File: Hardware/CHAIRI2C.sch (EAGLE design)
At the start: 23 parts, among them IC1 DS3502, IC2 DS3502, J2 OUTPUT, J4 M06-PLAIN

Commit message: Changed I2C pullups from 10K to 4K7. Moved designators to improve readability.
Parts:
- R10, R9: value 22K -> 4K7
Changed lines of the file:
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@@
 <part name="GND7" library="SuperHouse-SupplySymbols" library_urn="urn:adsk.eagle:library:11790503" deviceset="GND" device=""/>
 <part name="P+4" library="SuperHouse-SupplySymbols" library_urn="urn:adsk.eagle:library:11790503" deviceset="VCC" device=""/>
-<part name="R9" library="SuperHouse-DiscreteSemi" library_urn="urn:adsk.eagle:library:11768461" deviceset="RESISTOR" device="0603" package3d_urn="urn:adsk.eagle:package:11768543/2" value="22K"/>
-<part name="R10" library="SuperHouse-DiscreteSemi" library_urn="urn:adsk.eagle:library:11768461" deviceset="RESISTOR" device="0603" package3d_urn="urn:adsk.eagle:package:11768543/2" value="22K"/>
+<part name="R9" library="SuperHouse-DiscreteSemi" library_urn="urn:adsk.eagle:library:11768461" deviceset="RESISTOR" device="0603" package3d_urn="urn:adsk.eagle:package:11768543/2" value="4K7"/>
+<part name="R10" library="SuperHouse-DiscreteSemi" library_urn="urn:adsk.eagle:library:11768461" deviceset="RESISTOR" device="0603" package3d_urn="urn:adsk.eagle:package:11768543/2" value="4K7"/>
 <part name="U$2" library="SuperHouse-Jumpers" library_urn="urn:adsk.eagle:library:12190622" deviceset="SJC" device="-NORMAL" package3d_urn="urn:adsk.eagle:package:7066342/1" value="PU"/>
 <part name="U$3" library="SuperHouse-Jumpers" library_urn="urn:adsk.eagle:library:12190622" deviceset="SJC" device="-NORMAL" package3d_urn="urn:adsk.eagle:package:7066342/1" value="PU"/>

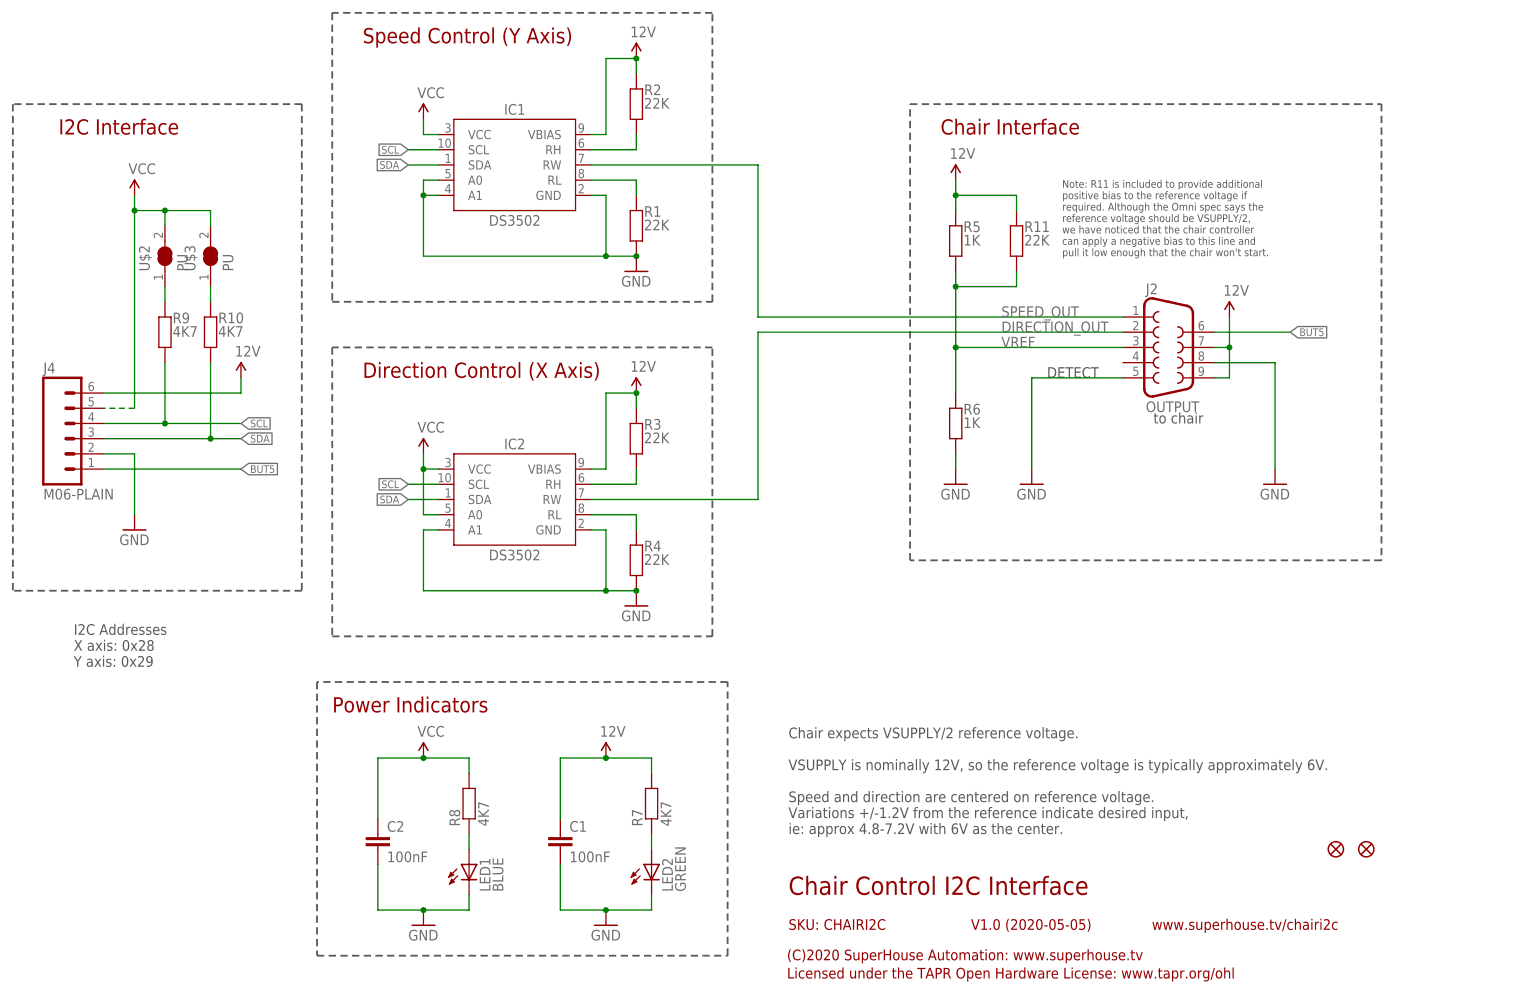
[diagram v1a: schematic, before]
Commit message: Renumbered parts to simplify production setup.
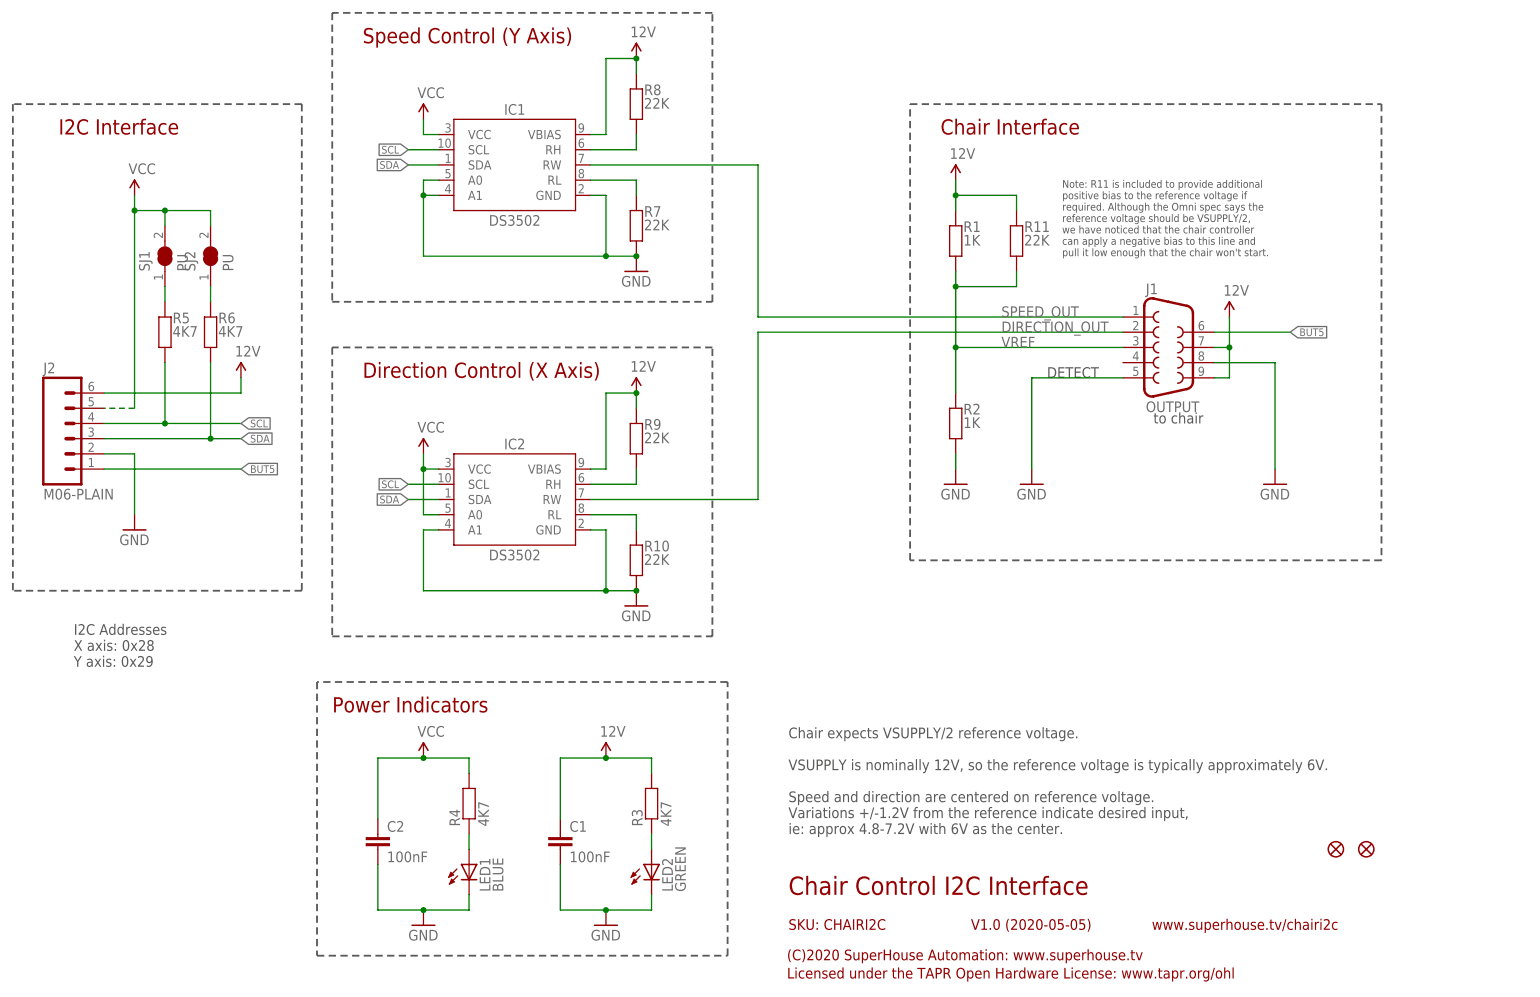
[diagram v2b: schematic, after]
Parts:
- removed J4: M06-PLAIN, SuperHouse-Connectors:M06-PLAIN
- added J1: OUTPUT, SuperHouse-Connectors:DB9-PCB-SOCKET
- J2: value OUTPUT -> M06-PLAIN; device SuperHouse-Connectors:DB9-PCB-SOCKET -> SuperHouse-Connectors:M06-PLAIN
- R1, R2: value 22K -> 1K
- R10, R7, R8, R9: value 4K7 -> 22K
- R3, R4: value 22K -> 4K7
- R5, R6: value 1K -> 4K7
- renumbered U$2 to SJ1, U$3 to SJ2, U$8 to FID1, U$9 to FID2
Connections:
- net 12V: now also J1.7, J1.9, J2.6, R1.2, R8.2, R9.2; no longer J2.7, J2.9, J4.6, R2.2, R5.2, R7.2
- net BUT5: now also J1.6, J2.1; no longer J2.6, J4.1
- net DIRECTION_OUT: now also J1.2; no longer J2.2
- net GND: now also J1.5, J1.8, J2.2, R10.1, R2.1, R7.1; no longer J2.5, J2.8, J4.2, R1.1, R4.1, R6.1
- net N$1: now also R5.2; no longer R9.2
- net N$15: now also R10.2; no longer R4.2
- net N$2: now also R8.1; no longer R2.1
- net N$3: now also R9.1; no longer R3.1
- net N$4: now also R7.2; no longer R1.2
- net N$5: now also R4.1; no longer R8.1
- net N$6: now also R3.1; no longer R7.1
- net N$8: now also R6.2; no longer R10.2
- net SCL: now also J2.4, R5.1; no longer J4.4, R9.1
- net SDA: now also J2.3, R6.1; no longer J4.3, R10.1
- net SPEED_OUT: now also J1.1; no longer J2.1
- net VCC: now also J2.5, R4.2; no longer J4.5, R8.2
- net VREF: now also J1.3, R1.1, R2.2; no longer J2.3, R5.1, R6.2
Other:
- moved on the sheet: R1, R10, R2, R3, R4, R5, R6, R7, R8, R9

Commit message: Changed output range resistors from 22K to 0R.
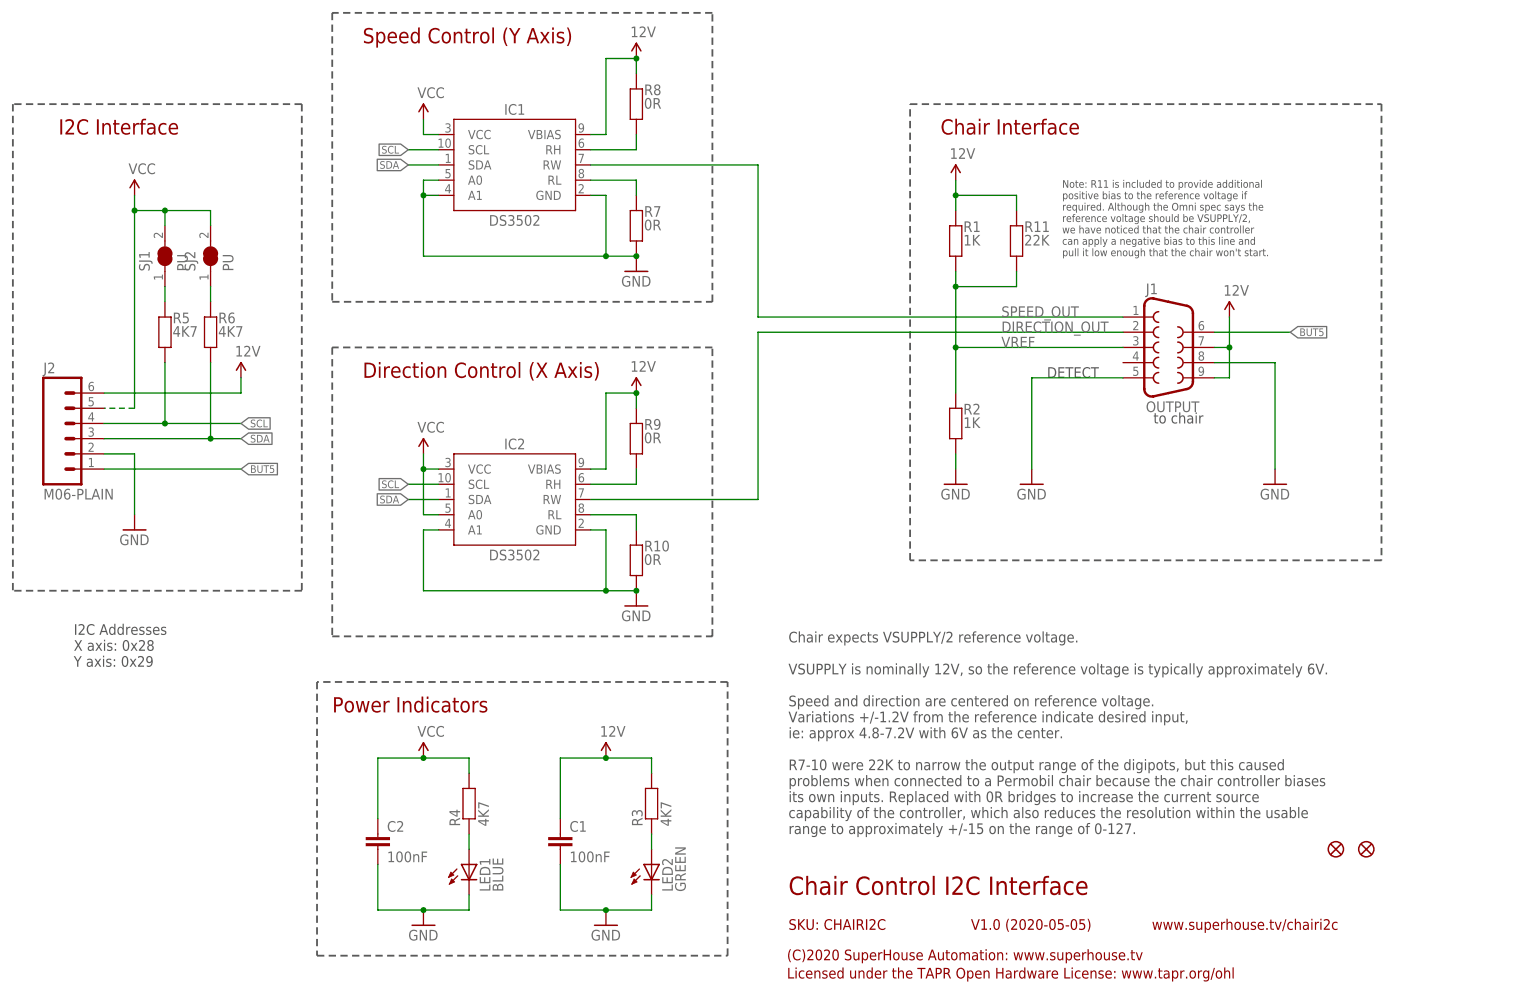
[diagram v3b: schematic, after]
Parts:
- R10, R7, R8, R9: value 22K -> 0R
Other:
- note added: "Chair expects VSUPPLY/2 reference voltage. VSUPPLY is nominally 12V, so the reference voltage is typically approximately 6V. Speed and direction are centered on reference voltage. Variations +/-1.2V from the reference indicate desired input, ie: approx 4.8-7.2V with 6V as the center. R7-10 were 22K to narrow the output range of the digipots, but this caused problems when connected to a Permobil c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"
- note removed: "Chair expects VSUPPLY/2 reference voltage. VSUPPLY is nominally 12V, so the reference voltage is typically approximately 6V. Speed and direction are centered on reference voltage. Variations +/-1.2V from the reference indicate desired input, ie: approx 4.8-7.2V with 6V as the center."
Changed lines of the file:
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@@
 <part name="IC2" library="SuperHouse-ICs" library_urn="urn:adsk.eagle:library:11768868" deviceset="DS3502" device="" package3d_urn="urn:adsk.eagle:package:20803613/2"/>
 <part name="GND2" library="SuperHouse-SupplySymbols" library_urn="urn:adsk.eagle:library:11790503" deviceset="GND" device=""/>
-<part name="R7" library="SuperHouse-DiscreteSemi" library_urn="urn:adsk.eagle:library:11768461" deviceset="RESISTOR" device="0603" package3d_urn="urn:adsk.eagle:package:11768543/2" value="22K"/>
-<part name="R8" library="SuperHouse-DiscreteSemi" library_urn="urn:adsk.eagle:library:11768461" deviceset="RESISTOR" device="0603" package3d_urn="urn:adsk.eagle:package:11768543/2" value="22K"/>
+<part name="R7" library="SuperHouse-DiscreteSemi" library_urn="urn:adsk.eagle:library:11768461" deviceset="RESISTOR" device="0603" package3d_urn="urn:adsk.eagle:package:11768543/2" value="0R"/>
+<part name="R8" library="SuperHouse-DiscreteSemi" library_urn="urn:adsk.eagle:library:11768461" deviceset="RESISTOR" device="0603" package3d_urn="urn:adsk.eagle:package:11768543/2" value="0R"/>
 <part name="GND4" library="SuperHouse-SupplySymbols" library_urn="urn:adsk.eagle:library:11790503" deviceset="GND" device=""/>
-<part name="R9" library="SuperHouse-DiscreteSemi" library_urn="urn:adsk.eagle:library:11768461" deviceset="RESISTOR" device="0603" package3d_urn="urn:adsk.eagle:package:11768543/2" value="22K"/>
-<part name="R10" library="SuperHouse-DiscreteSemi" library_urn="urn:adsk.eagle:library:11768461" deviceset="RESISTOR" device="0603" package3d_urn="urn:adsk.eagle:package:11768543/2" value="22K"/>
+<part name="R9" library="SuperHouse-DiscreteSemi" library_urn="urn:adsk.eagle:library:11768461" deviceset="RESISTOR" device="0603" package3d_urn="urn:adsk.eagle:package:11768543/2" value="0R"/>
+<part name="R10" library="SuperHouse-DiscreteSemi" library_urn="urn:adsk.eagle:library:11768461" deviceset="RESISTOR" device="0603" package3d_urn="urn:adsk.eagle:package:11768543/2" value="0R"/>
 <part name="R1" library="SuperHouse-DiscreteSemi" library_urn="urn:adsk.eagle:library:11768461" deviceset="RESISTOR" device="0603" package3d_urn="urn:adsk.eagle:package:11768543/2" value="1K"/>
 <part name="R2" library="SuperHouse-DiscreteSemi" library_urn="urn:adsk.eagle:library:11768461" deviceset="RESISTOR" device="0603" package3d_urn="urn:adsk.eagle:package:11768543/2" value="1K"/>
@@
 Speed and direction are centered on reference voltage.
 Variations +/-1.2V from the reference indicate desired input,
-ie: approx 4.8-7.2V with 6V as the center.</text>
+ie: approx 4.8-7.2V with 6V as the center.
+R7-10 were 22K to narrow the output range of the digipots, but this caused
+problems when connected to a Permobil chair because the chair controller biases
+its own inputs. Replaced with 0R bridges to increase the current source
+capability of the controller, which also reduces the resolution within the usable
+range to approximately +/-15 on the range of 0-127.</text>
 <text x="187.96" y="127" size="1.27" layer="97">Note: R11 is included to provide additional
 positive bias to the reference voltage if
